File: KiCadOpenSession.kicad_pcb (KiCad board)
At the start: 2 copper layers, 25.4 x 68.6 mm, 6 parts, among them J1 Conn_02x25_Odd_Even, U1 25LCxxx, U2 74HC4051, U3 25LCxxx

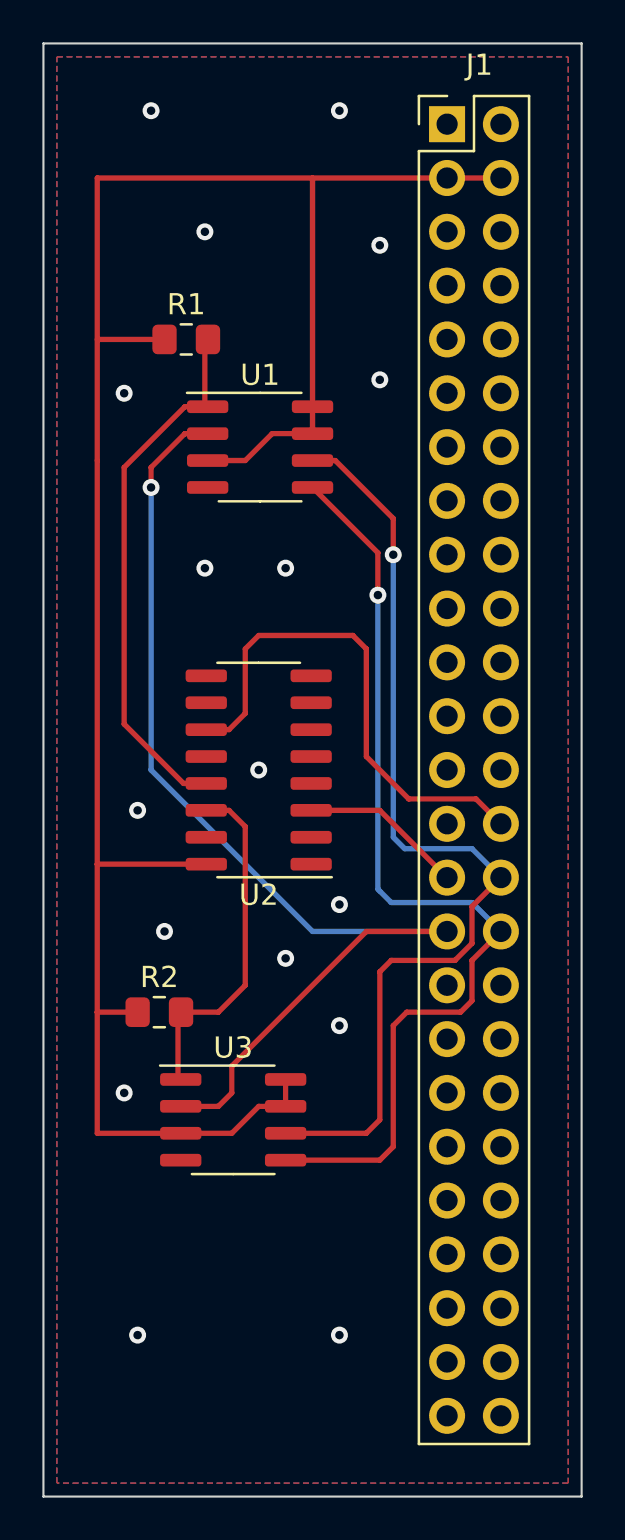
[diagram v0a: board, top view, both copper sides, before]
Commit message: Add smoothing capacitors
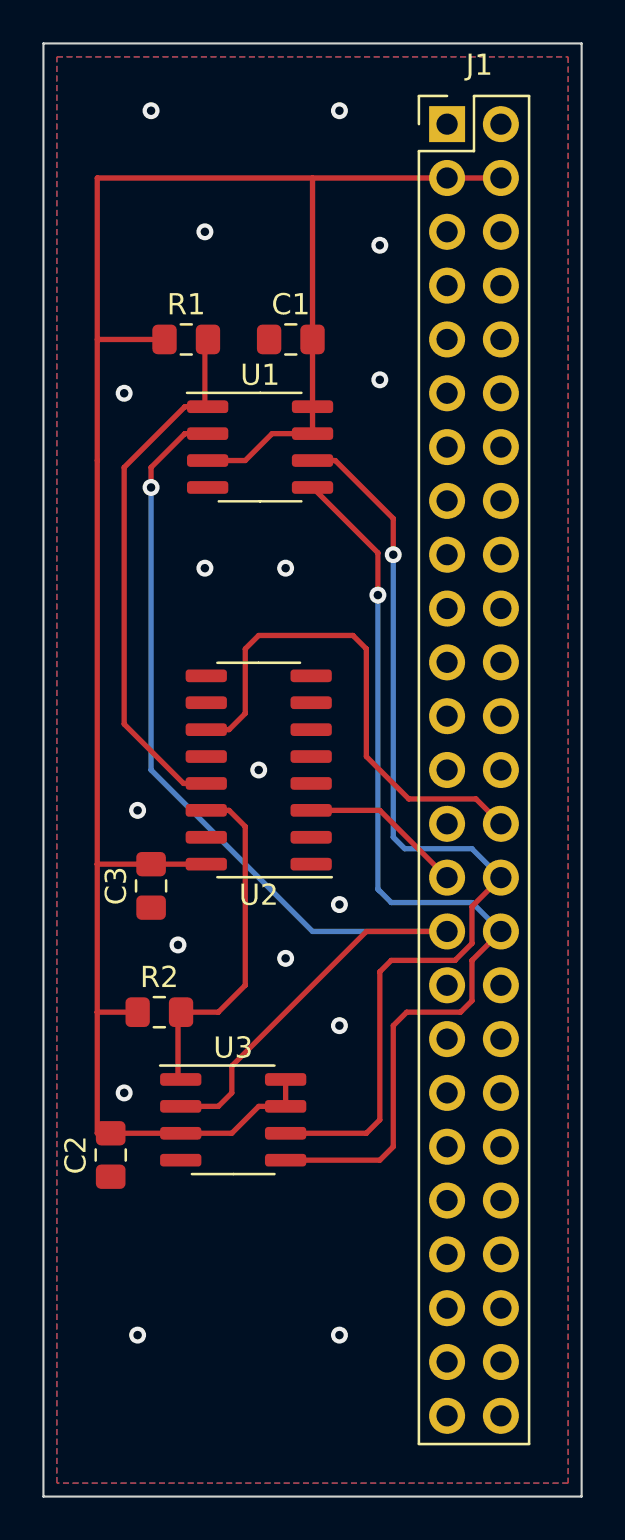
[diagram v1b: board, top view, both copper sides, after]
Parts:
- added C1: C, Capacitor_SMD:C_0805_2012Metric_Pad1.15x1.40mm_HandSolder, F.Cu at (151.4, 90.2)
- added C2: C, Capacitor_SMD:C_0805_2012Metric_Pad1.15x1.40mm_HandSolder, F.Cu at (142.9, 128.7)
- added C3: C, Capacitor_SMD:C_0805_2012Metric_Pad1.15x1.40mm_HandSolder, F.Cu at (144.8, 116.0)
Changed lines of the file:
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@@
-(kicad_pcb (version 20171130) (host pcbnew 5.1.6-c6e7f7d~87~ubuntu18.04.1)
+(kicad_pcb (version 20171130) (host pcbnew "(5.1.4)-1")
   (general
     (thickness 1.6)
@@
     (tracks 107)
     (zones 0)
-    (modules 6)
+    (modules 9)
     (nets 57)
   )
@@
     (add_net VDD)
   )
+  (module Capacitor_SMD:C_0805_2012Metric_Pad1.15x1.40mm_HandSolder (layer F.Cu)
+    (at 144.78 115.96 90)
+    (descr "Capacitor SMD 0805 (2012 Metric), square (rectangular) end terminal, IPC_7351 nominal with elongated pad for handsoldering. (Body size source: https://docs.google.com/spreadsheets/d/1BsfQQcO9C6DZCsRaXUlFlo91Tg2WpOkGARC1WS5S8t0/edit?usp=sharing), generated with kicad-footprint-generator")
+    (tags "capacitor handsolder")
+    (attr smd)
+    (fp_text reference C3 (at 0 -1.65 90) (layer F.SilkS)
+      (effects (font (size 1 1) (thickness 0.15)))
+    )
+    (fp_text value C (at 0 1.65 90) (layer F.Fab)
+      (effects (font (size 1 1) (thickness 0.15)))
+    )
+    (fp_text user %R (at 0 0 90) (layer F.Fab)
+      (effects (font (size 0.5 0.5) (thickness 0.08)))
+    )
+    (fp_line (start 1.85 0.95) (end -1.85 0.95) (layer F.CrtYd) (width 0.05))
+    (fp_line (start 1.85 -0.95) (end 1.85 0.95) (layer F.CrtYd) (width 0.05))
+    (fp_line (start -1.85 -0.95) (end 1.85 -0.95) (layer F.CrtYd) (width 0.05))
+    (fp_line (start -1.85 0.95) (end -1.85 -0.95) (layer F.CrtYd) (width 0.05))
+    (fp_line (start -0.261252 0.71) (end 0.261252 0.71) (layer F.SilkS) (width 0.12))
+    (fp_line (start -0.261252 -0.71) (end 0.261252 -0.71) (layer F.SilkS) (width 0.12))
+    (fp_line (start 1 0.6) (end -1 0.6) (layer F.Fab) (width 0.1))
+    (fp_line (start 1 -0.6) (end 1 0.6) (layer F.Fab) (width 0.1))
+    (fp_line (start -1 -0.6) (end 1 -0.6) (layer F.Fab) (width 0.1))
+    (fp_line (start -1 0.6) (end -1 -0.6) (layer F.Fab) (width 0.1))
+    (pad 2 smd roundrect (at 1.025 0 90) (size 1.15 1.4) (layers F.Cu F.Paste F.Mask) (roundrect_rratio 0.217391)
+      (net 56 VDD))
+    (pad 1 smd roundrect (at -1.025 0 90) (size 1.15 1.4) (layers F.Cu F.Paste F.Mask) (roundrect_rratio 0.217391)
+      (net 40 GND))
+    (model ${KISYS3DMOD}/Capacitor_SMD.3dshapes/C_0805_2012Metric.wrl
+      (at (xyz 0 0 0))
+      (scale (xyz 1 1 1))
+      (rotate (xyz 0 0 0))
+    )
+  )
+  (module Capacitor_SMD:C_0805_2012Metric_Pad1.15x1.40mm_HandSolder (layer F.Cu)
+    (at 142.875 128.66 90)
+    (descr "Capacitor SMD 0805 (2012 Metric), square (rectangular) end terminal, IPC_7351 nominal with elongated pad for handsoldering. (Body size source: https://docs.google.com/spreadsheets/d/1BsfQQcO9C6DZCsRaXUlFlo91Tg2WpOkGARC1WS5S8t0/edit?usp=sharing), generated with kicad-footprint-generator")
+    (tags "capacitor handsolder")
+    (attr smd)
+    (fp_text reference C2 (at 0 -1.65 90) (layer F.SilkS)
+      (effects (font (size 1 1) (thickness 0.15)))
+    )
+    (fp_text value C (at 0 1.65 90) (layer F.Fab)
+      (effects (font (size 1 1) (thickness 0.15)))
+    )
+    (fp_text user %R (at 0 0 90) (layer F.Fab)
+      (effects (font (size 0.5 0.5) (thickness 0.08)))
+    )
+    (fp_line (start 1.85 0.95) (end -1.85 0.95) (layer F.CrtYd) (width 0.05))
+    (fp_line (start 1.85 -0.95) (end 1.85 0.95) (layer F.CrtYd) (width 0.05))
+    (fp_line (start -1.85 -0.95) (end 1.85 -0.95) (layer F.CrtYd) (width 0.05))
+    (fp_line (start -1.85 0.95) (end -1.85 -0.95) (layer F.CrtYd) (width 0.05))
+    (fp_line (start -0.261252 0.71) (end 0.261252 0.71) (layer F.SilkS) (width 0.12))
+    (fp_line (start -0.261252 -0.71) (end 0.261252 -0.71) (layer F.SilkS) (width 0.12))
+    (fp_line (start 1 0.6) (end -1 0.6) (layer F.Fab) (width 0.1))
+    (fp_line (start 1 -0.6) (end 1 0.6) (layer F.Fab) (width 0.1))
+    (fp_line (start -1 -0.6) (end 1 -0.6) (layer F.Fab) (width 0.1))
+    (fp_line (start -1 0.6) (end -1 -0.6) (layer F.Fab) (width 0.1))
+    (pad 2 smd roundrect (at 1.025 0 90) (size 1.15 1.4) (layers F.Cu F.Paste F.Mask) (roundrect_rratio 0.217391)
+      (net 56 VDD))
+    (pad 1 smd roundrect (at -1.025 0 90) (size 1.15 1.4) (layers F.Cu F.Paste F.Mask) (roundrect_rratio 0.217391)
+      (net 40 GND))
+    (model ${KISYS3DMOD}/Capacitor_SMD.3dshapes/C_0805_2012Metric.wrl
+      (at (xyz 0 0 0))
+      (scale (xyz 1 1 1))
+      (rotate (xyz 0 0 0))
+    )
+  )
+  (module Capacitor_SMD:C_0805_2012Metric_Pad1.15x1.40mm_HandSolder (layer F.Cu)
+    (at 151.375 90.17)
+    (descr "Capacitor SMD 0805 (2012 Metric), square (rectangular) end terminal, IPC_7351 nominal with elongated pad for handsoldering. (Body size source: https://docs.google.com/spreadsheets/d/1BsfQQcO9C6DZCsRaXUlFlo91Tg2WpOkGARC1WS5S8t0/edit?usp=sharing), generated with kicad-footprint-generator")
+    (tags "capacitor handsolder")
+    (attr smd)
+    (fp_text reference C1 (at 0 -1.65) (layer F.SilkS)
+      (effects (font (size 1 1) (thickness 0.15)))
+    )
+    (fp_text value C (at 0 1.65) (layer F.Fab)
+      (effects (font (size 1 1) (thickness 0.15)))
+    )
+    (fp_text user %R (at 0 0) (layer F.Fab)
+      (effects (font (size 0.5 0.5) (thickness 0.08)))
+    )
+    (fp_line (start 1.85 0.95) (end -1.85 0.95) (layer F.CrtYd) (width 0.05))
+    (fp_line (start 1.85 -0.95) (end 1.85 0.95) (layer F.CrtYd) (width 0.05))
+    (fp_line (start -1.85 -0.95) (end 1.85 -0.95) (layer F.CrtYd) (width 0.05))
+    (fp_line (start -1.85 0.95) (end -1.85 -0.95) (layer F.CrtYd) (width 0.05))
+    (fp_line (start -0.261252 0.71) (end 0.261252 0.71) (layer F.SilkS) (width 0.12))
+    (fp_line (start -0.261252 -0.71) (end 0.261252 -0.71) (layer F.SilkS) (width 0.12))
+    (fp_line (start 1 0.6) (end -1 0.6) (layer F.Fab) (width 0.1))
+    (fp_line (start 1 -0.6) (end 1 0.6) (layer F.Fab) (width 0.1))
+    (fp_line (start -1 -0.6) (end 1 -0.6) (layer F.Fab) (width 0.1))
+    (fp_line (start -1 0.6) (end -1 -0.6) (layer F.Fab) (width 0.1))
+    (pad 2 smd roundrect (at 1.025 0) (size 1.15 1.4) (layers F.Cu F.Paste F.Mask) (roundrect_rratio 0.217391)
+      (net 56 VDD))
+    (pad 1 smd roundrect (at -1.025 0) (size 1.15 1.4) (layers F.Cu F.Paste F.Mask) (roundrect_rratio 0.217391)
+      (net 40 GND))
+    (model ${KISYS3DMOD}/Capacitor_SMD.3dshapes/C_0805_2012Metric.wrl
+      (at (xyz 0 0 0))
+      (scale (xyz 1 1 1))
+      (rotate (xyz 0 0 0))
+    )
+  )
   (module Package_SO:SOIC-8_3.9x4.9mm_P1.27mm (layer F.Cu)
     (at 148.655 127)
@@
   (via (at 143.51 92.71) (size 0.8) (drill 0.4) (layers F.Cu B.Cu) (net 40))
   (via (at 144.145 112.395) (size 0.8) (drill 0.4) (layers F.Cu B.Cu) (net 40))
-  (via (at 145.415 118.11) (size 0.8) (drill 0.4) (layers F.Cu B.Cu) (net 40))
+  (via (at 146.05 118.745) (size 0.8) (drill 0.4) (layers F.Cu B.Cu) (net 40))
   (via (at 153.67 122.555) (size 0.8) (drill 0.4) (layers F.Cu B.Cu) (net 40))
   (via (at 144.145 137.16) (size 0.8) (drill 0.4) (layers F.Cu B.Cu) (net 40))
